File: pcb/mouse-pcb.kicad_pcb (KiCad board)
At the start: 4 copper layers, 89.5 x 71.4 mm, 16 parts, among them J1 TYPE-C-31-M-12, SW1 D2FC-F-7N20M, SW2 D2FC-F-7N20M, SW3 D2FC-F-7N20M, U1 PAW3395-T6QU, U2 NRF54L15-QFAA-R

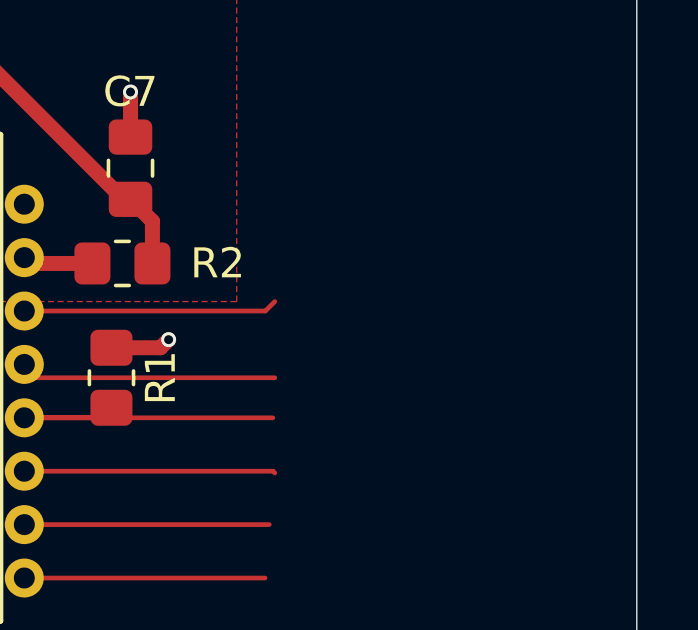
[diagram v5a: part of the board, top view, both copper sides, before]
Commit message: feat: 10mm logo added to library and pcb
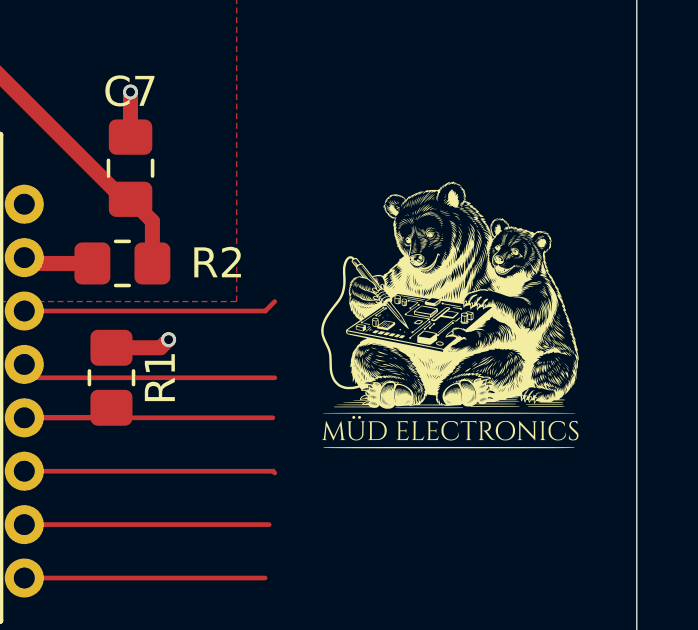
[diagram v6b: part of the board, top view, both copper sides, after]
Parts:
- added G***: LOGO, mouse_library:logo_10mm, F.Cu at (143.0, 83.0)

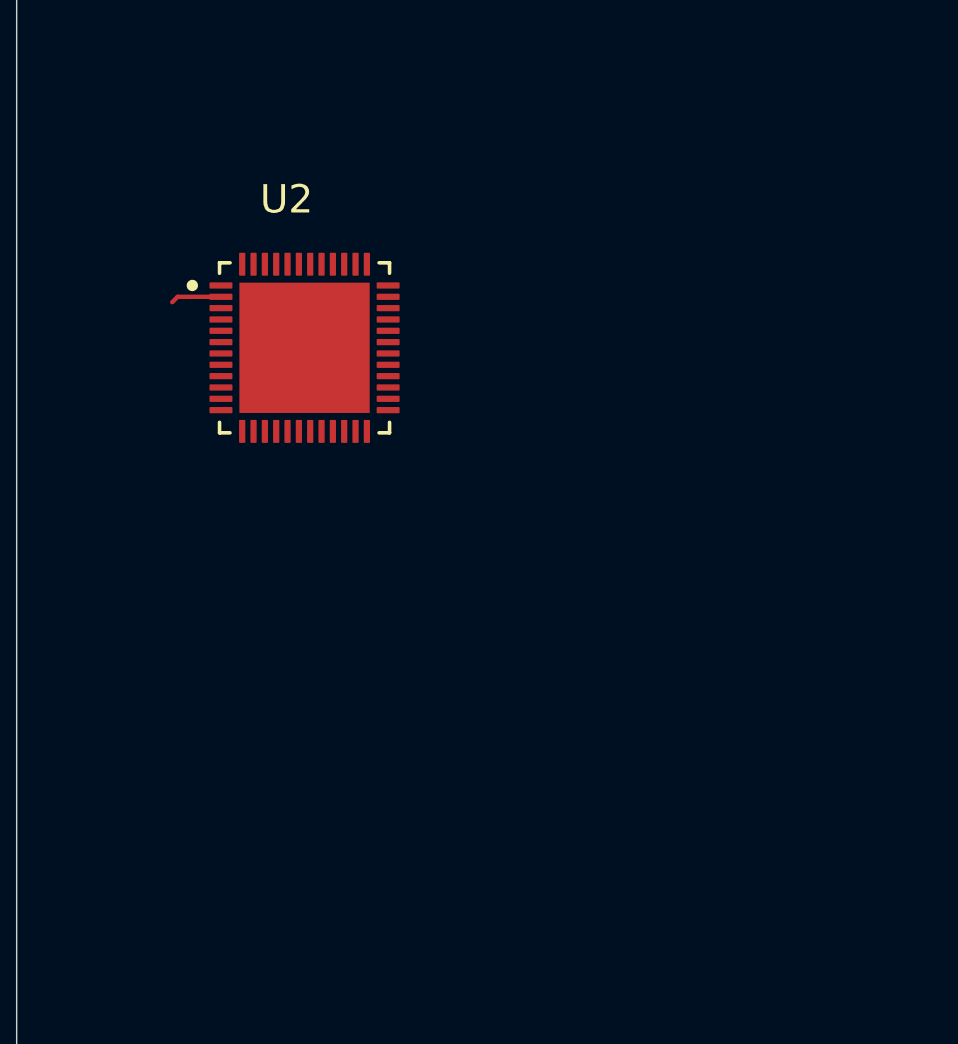
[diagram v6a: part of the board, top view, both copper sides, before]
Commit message: feat: common circuits for chip, antenna remaining
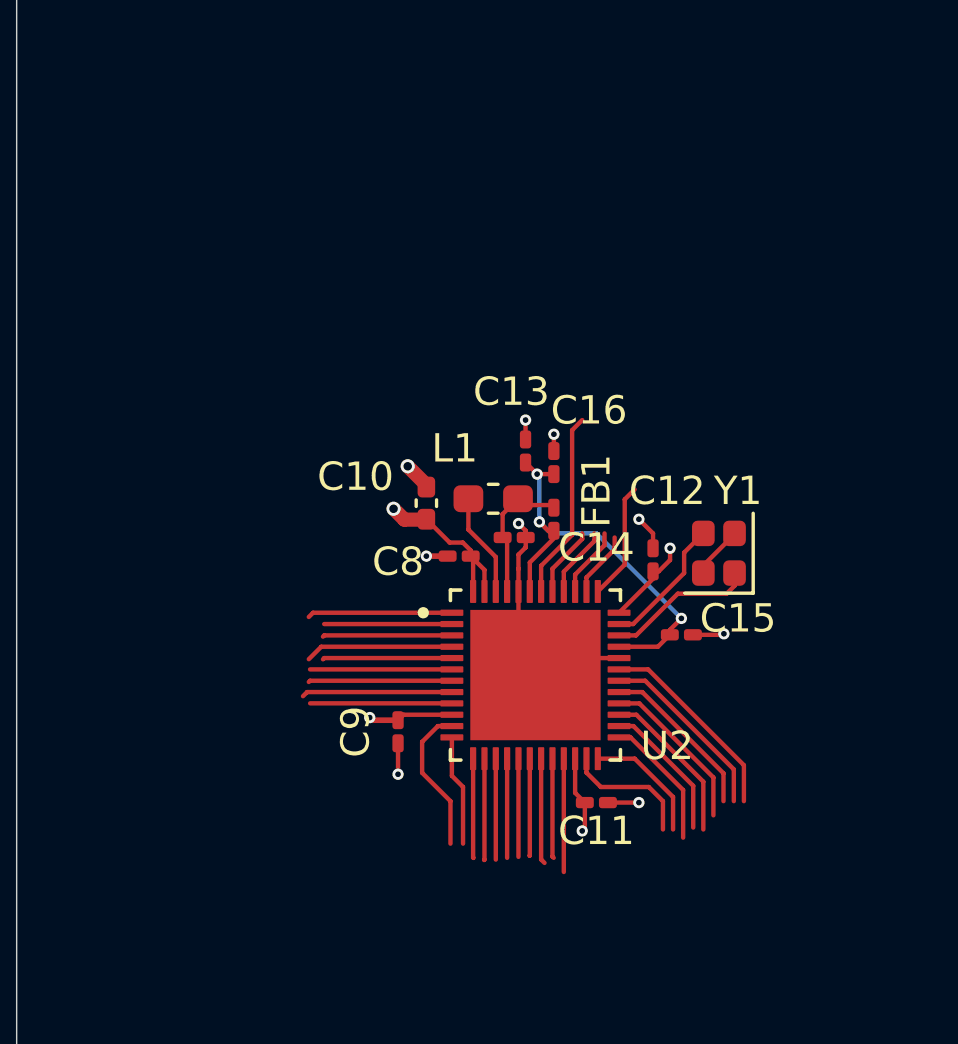
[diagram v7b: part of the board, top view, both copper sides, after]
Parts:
- added C10: 10uF, Capacitor_SMD:C_0402_1005Metric_Pad0.74x0.62mm_HandSolder, F.Cu at (74.2, 69.0)
- added C11: 100nF, Capacitor_SMD:C_0201_0603Metric_Pad0.64x0.40mm_HandSolder, F.Cu at (80.2, 79.5)
- added C12: 100nF, Capacitor_SMD:C_0201_0603Metric_Pad0.64x0.40mm_HandSolder, F.Cu at (82.2, 71.0)
- added C13: 2.2uf, Capacitor_SMD:C_0201_0603Metric_Pad0.64x0.40mm_HandSolder, F.Cu at (77.7, 67.1)
- added C14: 2.2uf, Capacitor_SMD:C_0201_0603Metric_Pad0.64x0.40mm_HandSolder, F.Cu at (77.2, 70.2)
- added C15: 2.2nf, Capacitor_SMD:C_0201_0603Metric_Pad0.64x0.40mm_HandSolder, F.Cu at (83.2, 73.6)
- added C16: 10nf, Capacitor_SMD:C_0201_0603Metric_Pad0.64x0.40mm_HandSolder, F.Cu at (78.7, 67.5)
- added C8: 100nF, Capacitor_SMD:C_0201_0603Metric_Pad0.64x0.40mm_HandSolder, F.Cu at (75.3, 70.9)
- added C9: 100nF, Capacitor_SMD:C_0201_0603Metric_Pad0.64x0.40mm_HandSolder, F.Cu at (73.2, 77.0)
- added FB1: FerriteBead, Inductor_SMD:L_0201_0603Metric_Pad0.64x0.40mm_HandSolder, F.Cu at (78.7, 69.5)
- added L1: 4.7uH, Inductor_SMD:L_0603_1608Metric_Pad1.05x0.95mm_HandSolder, F.Cu at (76.5, 68.8)
- added Y1: Crystal_GND24, Crystal:Crystal_SMD_2016-4Pin_2.0x1.6mm, F.Cu at (84.5, 70.8)
- moved U2 14.1 mm to (78.0, 75.0)
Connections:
- U2 pad 10: VDD -> +3V3
- U2 pad 22: VDD -> +3V3
- U2 pad 25: unconnected-(U2-SWDIO-Pad25) -> SWDIO
- U2 pad 26: unconnected-(U2-SWDCLK-Pad26) -> SWDCLK
- U2 pad 30: unconnected-(U2-~{RESET}-Pad30) -> RESET
- U2 pad 32: unconnected-(U2-VSS_PA-Pad32) -> GND
- U2 pad 33: unconnected-(U2-DECRF-Pad33) -> DECA
- U2 pad 34: unconnected-(U2-XC1-Pad34) -> Net-(U2-XC1)
- U2 pad 35: unconnected-(U2-XC2-Pad35) -> Net-(U2-XC2)
- U2 pad 36: VDD -> +3V3
- U2 pad 43: unconnected-(U2-DECA-Pad43) -> DECA
- U2 pad 44: VSS -> GND
- U2 pad 45: unconnected-(U2-DECD-Pad45) -> DECD
- U2 pad 46: unconnected-(U2-DCC-Pad46) -> DCC
- U2 pad 47: VDD -> +3V3
- U2 pad 48: VDD -> +3V3
- U2 pad 49: VSS -> GND
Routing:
- net GND: track 12.9 -> 31.2 mm, vias 8 -> 17
- net DECA: track 0.00 -> 14.9 mm, vias 0 -> 3
- net +3V3: track 9.74 -> 24.6 mm, vias 2 -> 6
- net unconnected-(U2-ANT-Pad31): track 0.00 -> 7.08 mm
- net unconnected-(U2-P1.14/RADIO(5)/AIN7-Pad42): track 0.00 -> 6.65 mm
- net RESET: track 0.00 -> 6.47 mm
- net unconnected-(U2-P0.04/GRTCLFCLKOUT-Pad29): track 0.00 -> 5.86 mm
- net unconnected-(U2-P0.03/GRTCPWM-Pad28): track 0.00 -> 5.75 mm
- net unconnected-(U2-P0.02-Pad27): track 0.00 -> 5.64 mm
- net unconnected-(U2-P1.07/ASI(1)/AIN3-Pad8): track 0.00 -> 5.31 mm
- net unconnected-(U2-P2.00-Pad11): track 0.00 -> 5.29 mm
- net Net-(U2-XC1): track 0.00 -> 5.25 mm
- net unconnected-(U2-P1.03/NFC2-Pad4): track 0.00 -> 5.23 mm
- net unconnected-(U2-P1.00/XL1-Pad1): track 0.00 -> 5.11 mm
- net unconnected-(U2-P1.06/ASO(1)/AIN2-Pad7): track 0.00 -> 5.07 mm
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
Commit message: feat: new micro, and antenna
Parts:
- removed C10: 10uF, Capacitor_SMD:C_0402_1005Metric_Pad0.74x0.62mm_HandSolder
- removed C11, C12, C8, C9: 100nF, Capacitor_SMD:C_0201_0603Metric_Pad0.64x0.40mm_HandSolder
- removed C13, C14: 2.2uf, Capacitor_SMD:C_0201_0603Metric_Pad0.64x0.40mm_HandSolder
- removed C15: 2.2nf, Capacitor_SMD:C_0201_0603Metric_Pad0.64x0.40mm_HandSolder
- removed C16: 10nf, Capacitor_SMD:C_0201_0603Metric_Pad0.64x0.40mm_HandSolder
- removed FB1: FerriteBead, Inductor_SMD:L_0201_0603Metric_Pad0.64x0.40mm_HandSolder
- removed L1: 4.7uH, Inductor_SMD:L_0603_1608Metric_Pad1.05x0.95mm_HandSolder
- removed Y1: Crystal_GND24, Crystal:Crystal_SMD_2016-4Pin_2.0x1.6mm
- added ANT1: ANT016008LCS2442MA2, mouse_library:ANT_ANT016008LCS2442MA2, F.Cu at (99.6, 96.2)
- C1, C2, C3, C4, C5, C6, C7: footprint Capacitor_SMD:C_0805_2012Metric_Pad1.18x1.45mm_HandSolder -> Capacitor_SMD:C_0805_2012Metric
- R1: footprint Resistor_SMD:R_0805_2012Metric_Pad1.20x1.40mm_HandSolder -> Resistor_SMD:R_0805_2012Metric
- R2: value 5R6 -> 6R8; footprint Resistor_SMD:R_0805_2012Metric_Pad1.20x1.40mm_HandSolder -> Resistor_SMD:R_0805_2012Metric
- U2: value NRF54L15-QFAA-R -> NRF52840-QIAA-R7; footprint mouse_library:QFN40P600X600X90-49N -> mouse_library:NORDIC_NRF52840-QIAA-R7
- moved U2 3.79 mm to (78.7, 78.8)
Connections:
- net +1V9 renamed +2V
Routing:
- net GND: track 31.2 -> 12.9 mm, vias 17 -> 8
- net DECA: track 14.9 -> 0.00 mm, vias 3 -> 0
- net +3V3: track 24.6 -> 9.74 mm, vias 6 -> 2
- net unconnected-(U2-ANT-Pad31): track 7.08 -> 0.00 mm
- net VBUS: track 0.00 -> 6.71 mm
- net unconnected-(U2-P1.14/RADIO(5)/AIN7-Pad42): track 6.65 -> 0.00 mm
- net RESET: track 6.47 -> 0.00 mm
- net unconnected-(U2-P0.04/GRTCLFCLKOUT-Pad29): track 5.86 -> 0.00 mm
- net unconnected-(U2-P0.03/GRTCPWM-Pad28): track 5.75 -> 0.00 mm
- net unconnected-(U2-P0.02-Pad27): track 5.64 -> 0.00 mm
- net unconnected-(U2-P1.07/ASI(1)/AIN3-Pad8): track 5.31 -> 0.00 mm
- net unconnected-(U2-P2.00-Pad11): track 5.29 -> 0.00 mm
- net Net-(U2-XC1): track 5.25 -> 0.00 mm
- net unconnected-(U2-P1.03/NFC2-Pad4): track 5.23 -> 0.00 mm
- net unconnected-(U2-P1.00/XL1-Pad1): track 5.11 -> 0.00 mm
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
